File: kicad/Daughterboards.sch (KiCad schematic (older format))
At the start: 6 parts

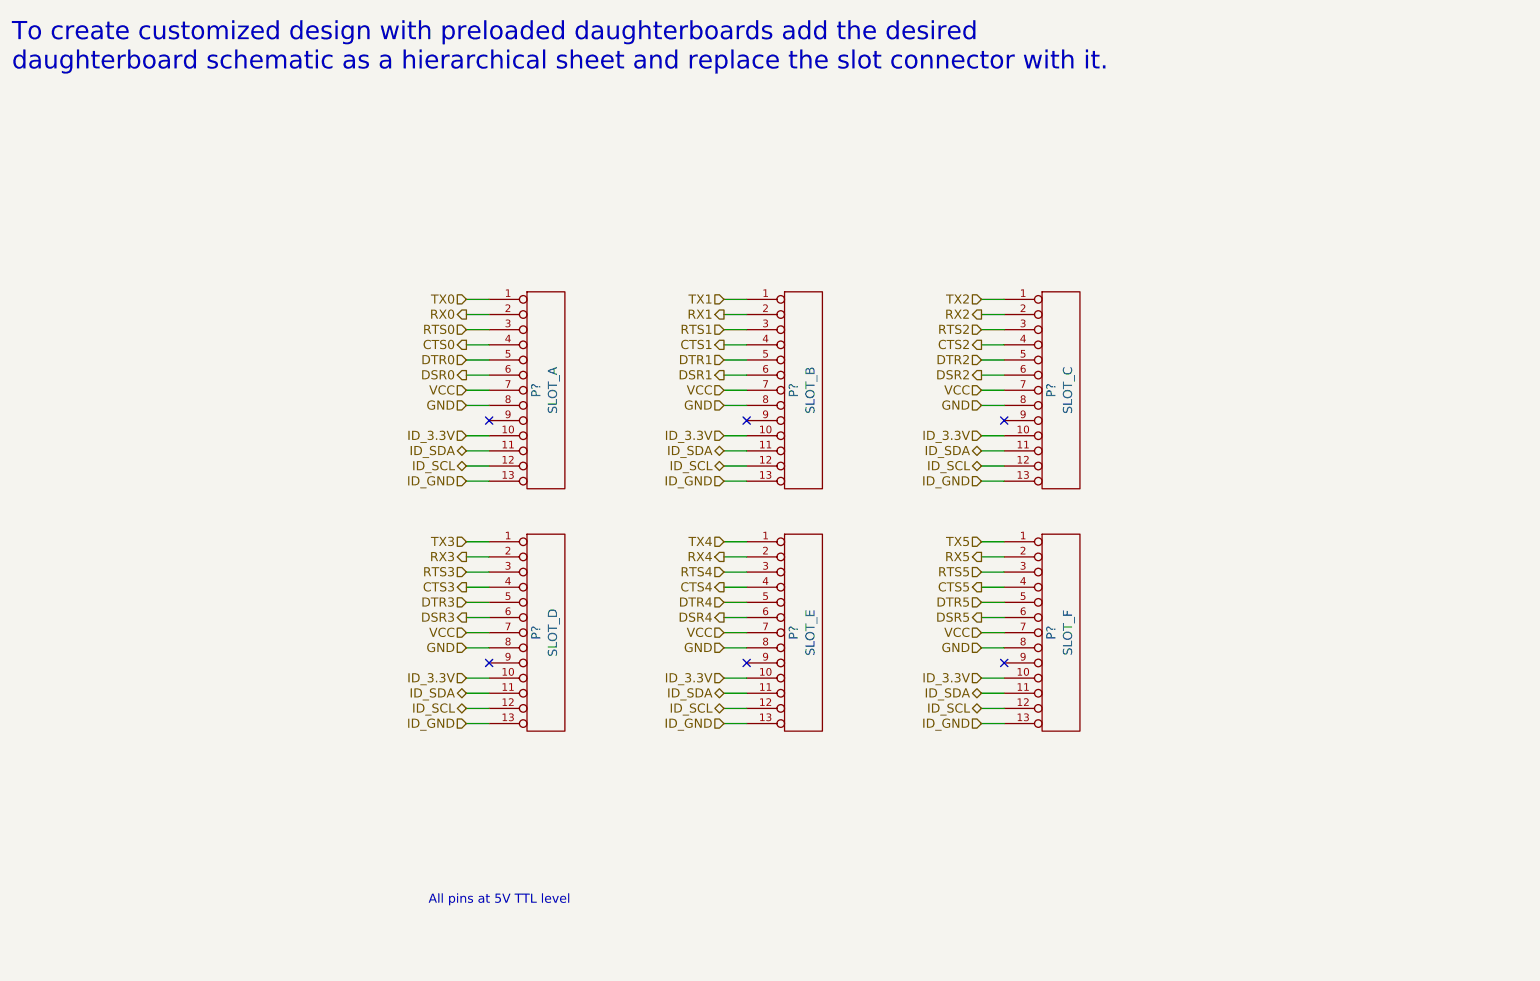
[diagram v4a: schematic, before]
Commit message: Completed PIC 18 USB sheet; Motherboard schematic done
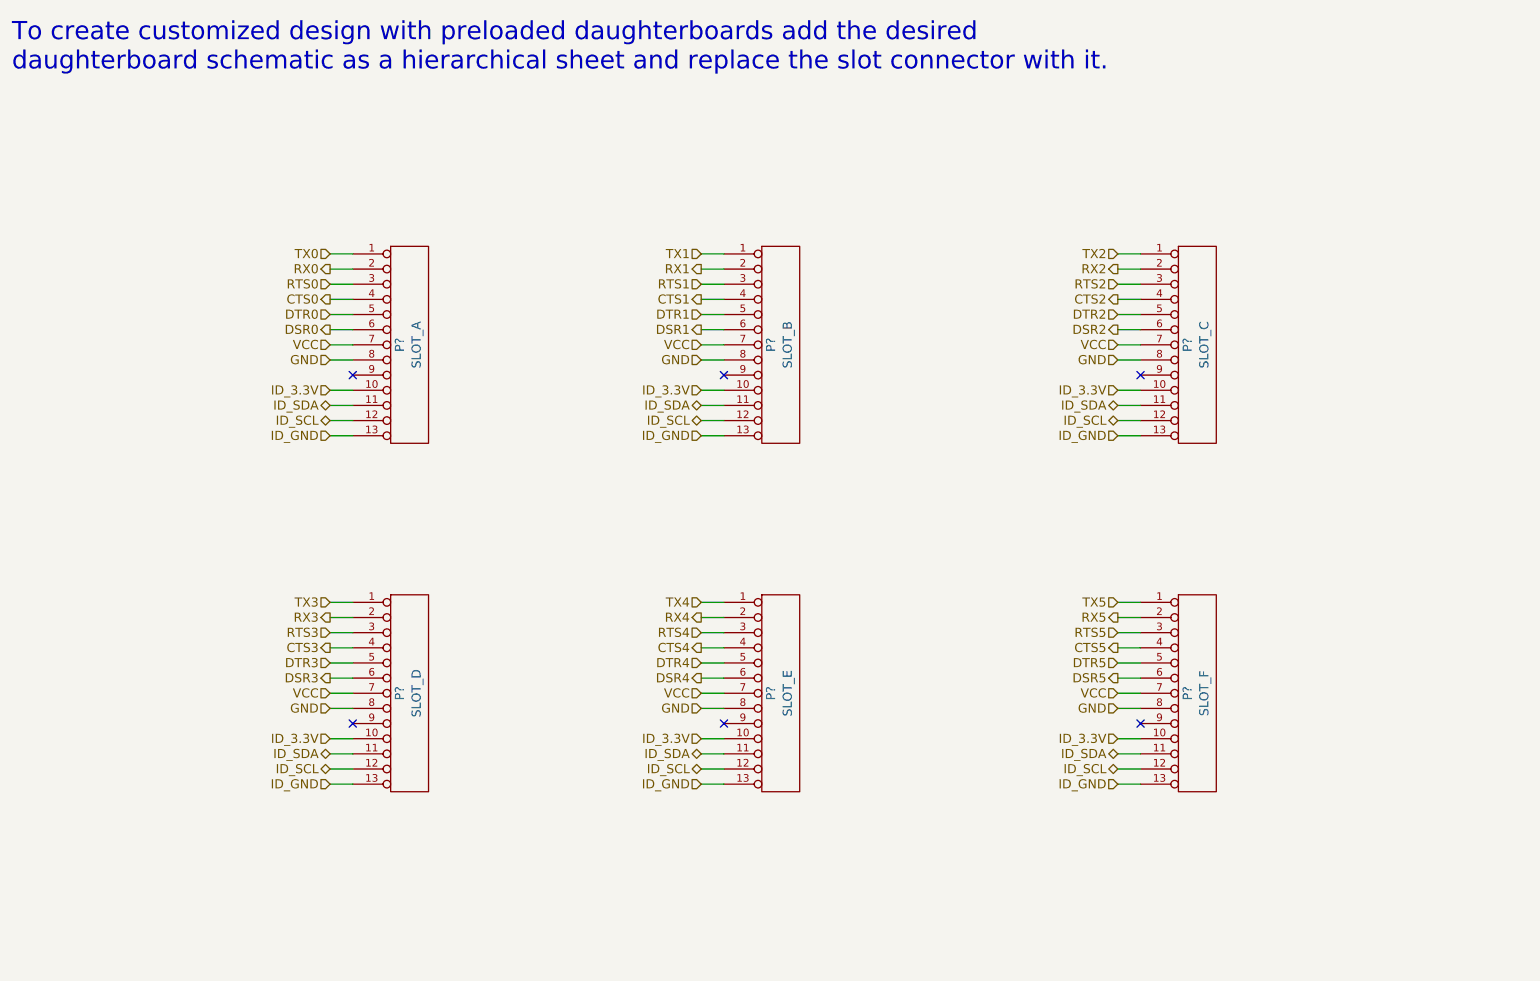
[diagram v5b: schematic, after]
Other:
- note removed: "All pins at 5V TTL level"
- moved on the sheet: P?

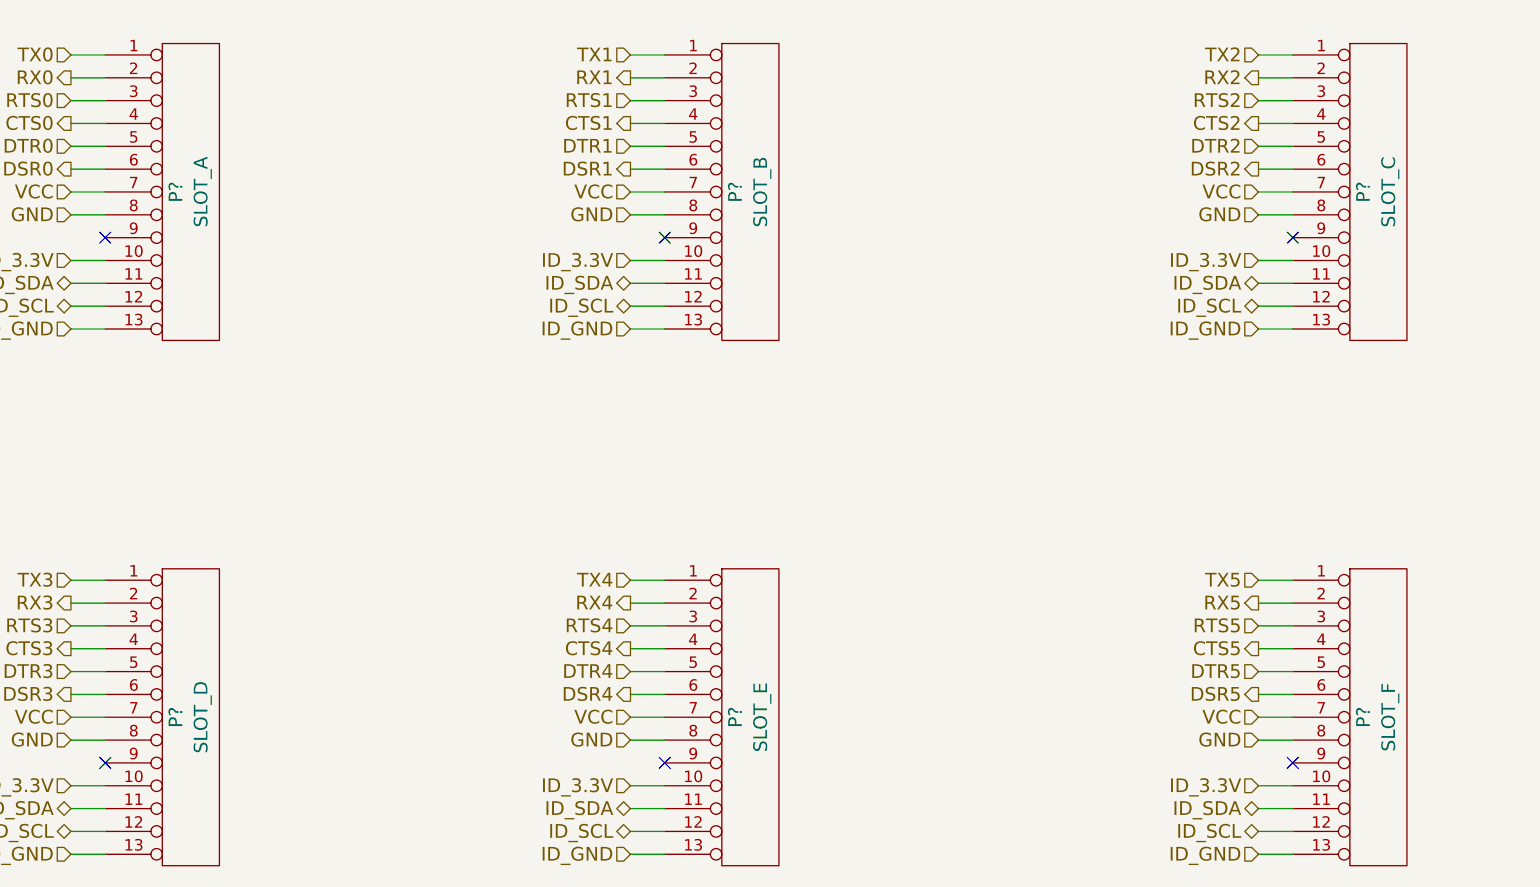
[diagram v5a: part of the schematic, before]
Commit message: Netlist DRC pass - fixed pins types, incorrect connections, added PWRFLAGS
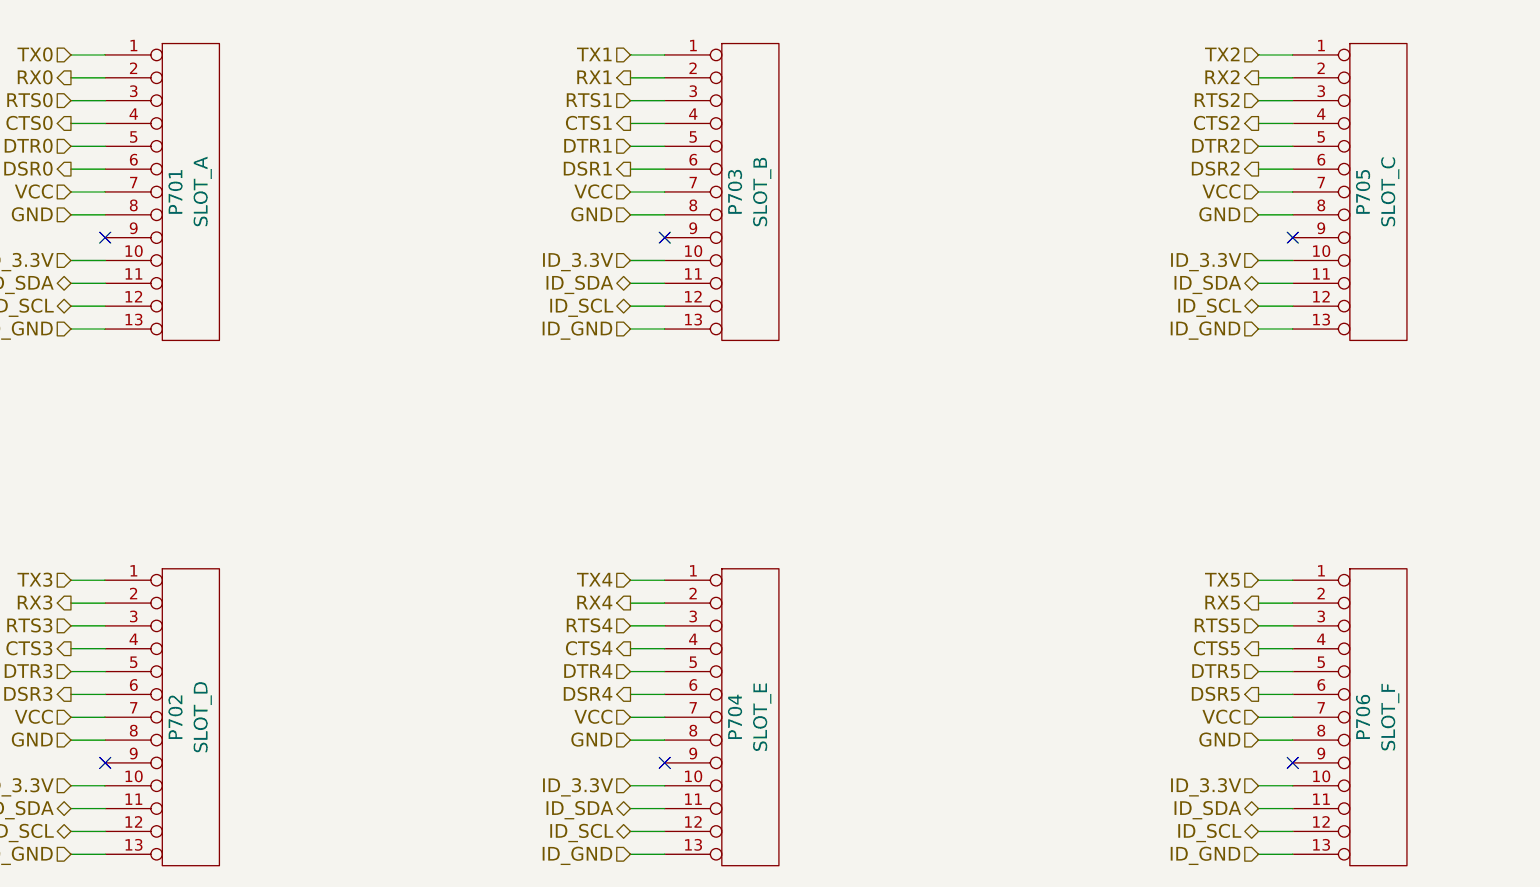
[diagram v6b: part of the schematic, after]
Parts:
- gave numbers to parts that had none: 6
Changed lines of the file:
@@
 	8300 5850 8450 5850
 $Comp
-L CONN_13 P?
+L CONN_13 P701
 U 1 1 53B751DE
 P 3600 2950
-F 0 "P?" V 3560 2950 60  0000 C CNN
+F 0 "P701" V 3560 2950 60  0000 C CNN
 F 1 "SLOT_A" V 3670 2950 60  0000 C CNN
 F 2 "" H 3600 2950 60  0000 C CNN
@@
 $EndComp
 $Comp
-L CONN_13 P?
+L CONN_13 P703
 U 1 1 53B751F7
 P 6050 2950
-F 0 "P?" V 6010 2950 60  0000 C CNN
+F 0 "P703" V 6010 2950 60  0000 C CNN
 F 1 "SLOT_B" V 6120 2950 60  0000 C CNN
 F 2 "" H 6050 2950 60  0000 C CNN
@@
 $EndComp
 $Comp
-L CONN_13 P?
+L CONN_13 P705
 U 1 1 53B75207
 P 8800 2950
-F 0 "P?" V 8760 2950 60  0000 C CNN
+F 0 "P705" V 8760 2950 60  0000 C CNN
 F 1 "SLOT_C" V 8870 2950 60  0000 C CNN
 F 2 "" H 8800 2950 60  0000 C CNN
@@
 $EndComp
 $Comp
-L CONN_13 P?
+L CONN_13 P702
 U 1 1 53B7520D
 P 3600 5250
-F 0 "P?" V 3560 5250 60  0000 C CNN
+F 0 "P702" V 3560 5250 60  0000 C CNN
 F 1 "SLOT_D" V 3670 5250 60  0000 C CNN
 F 2 "" H 3600 5250 60  0000 C CNN
@@
 $EndComp
 $Comp
-L CONN_13 P?
+L CONN_13 P704
 U 1 1 53B75213
 P 6050 5250
-F 0 "P?" V 6010 5250 60  0000 C CNN
+F 0 "P704" V 6010 5250 60  0000 C CNN
 F 1 "SLOT_E" V 6120 5250 60  0000 C CNN
 F 2 "" H 6050 5250 60  0000 C CNN
@@
 $EndComp
 $Comp
-L CONN_13 P?
+L CONN_13 P706
 U 1 1 53B75219
 P 8800 5250
-F 0 "P?" V 8760 5250 60  0000 C CNN
+F 0 "P706" V 8760 5250 60  0000 C CNN
 F 1 "SLOT_F" V 8870 5250 60  0000 C CNN
 F 2 "" H 8800 5250 60  0000 C CNN

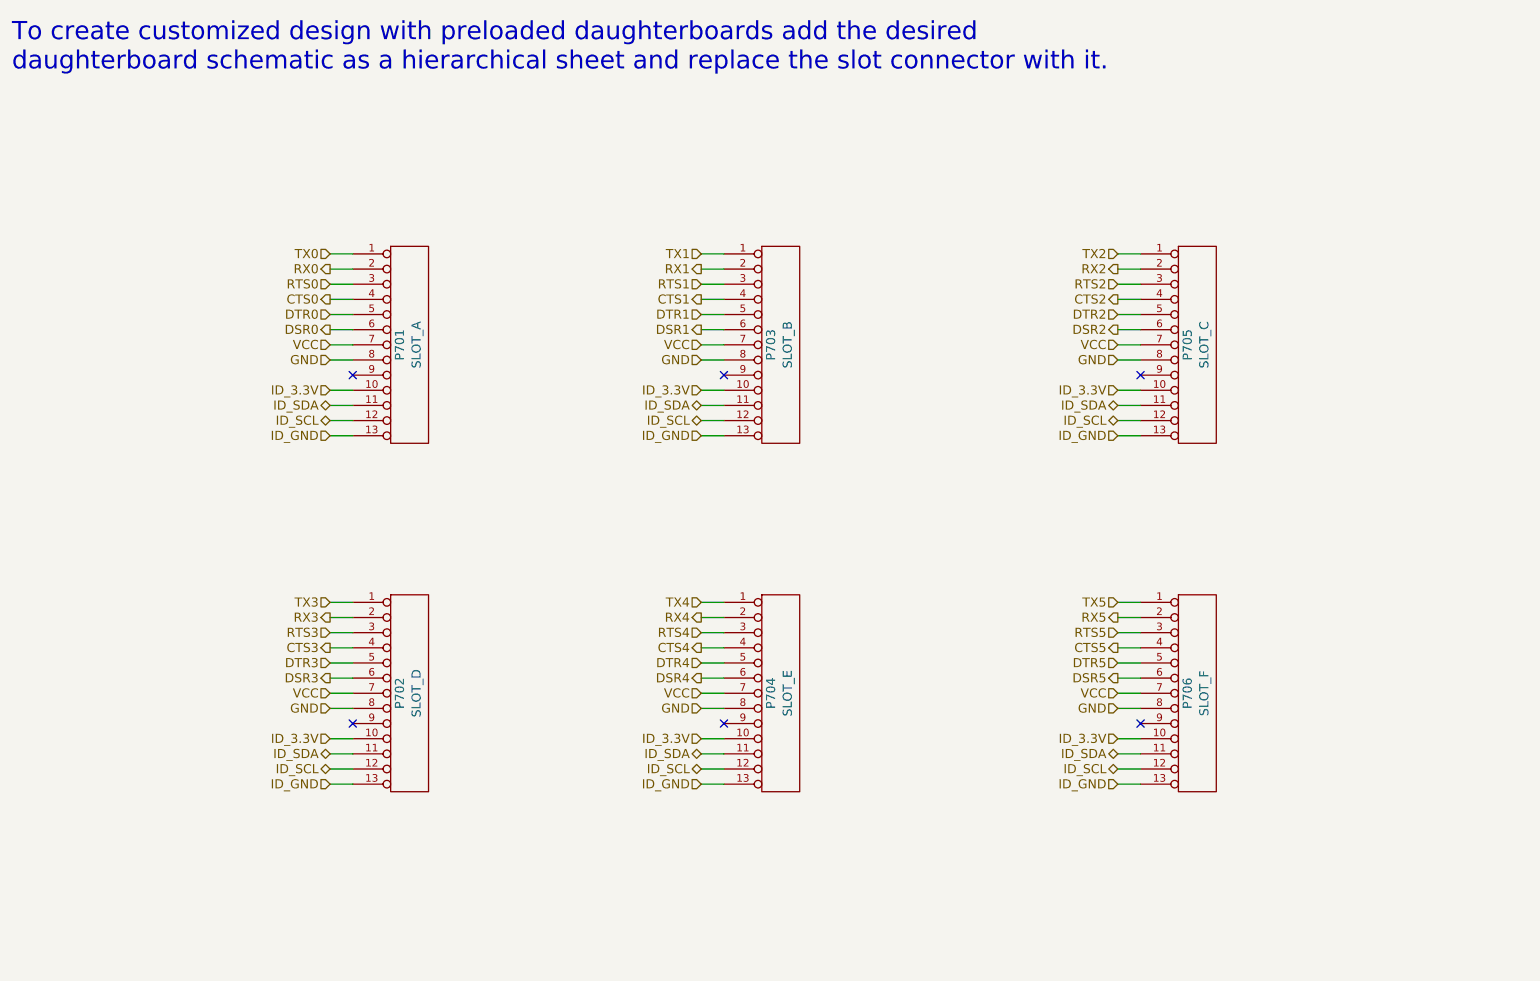
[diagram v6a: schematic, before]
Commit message: Fixed major flaw in autodetection circuit - daughterboard header pinout changed to set address of ROMs depending on slot
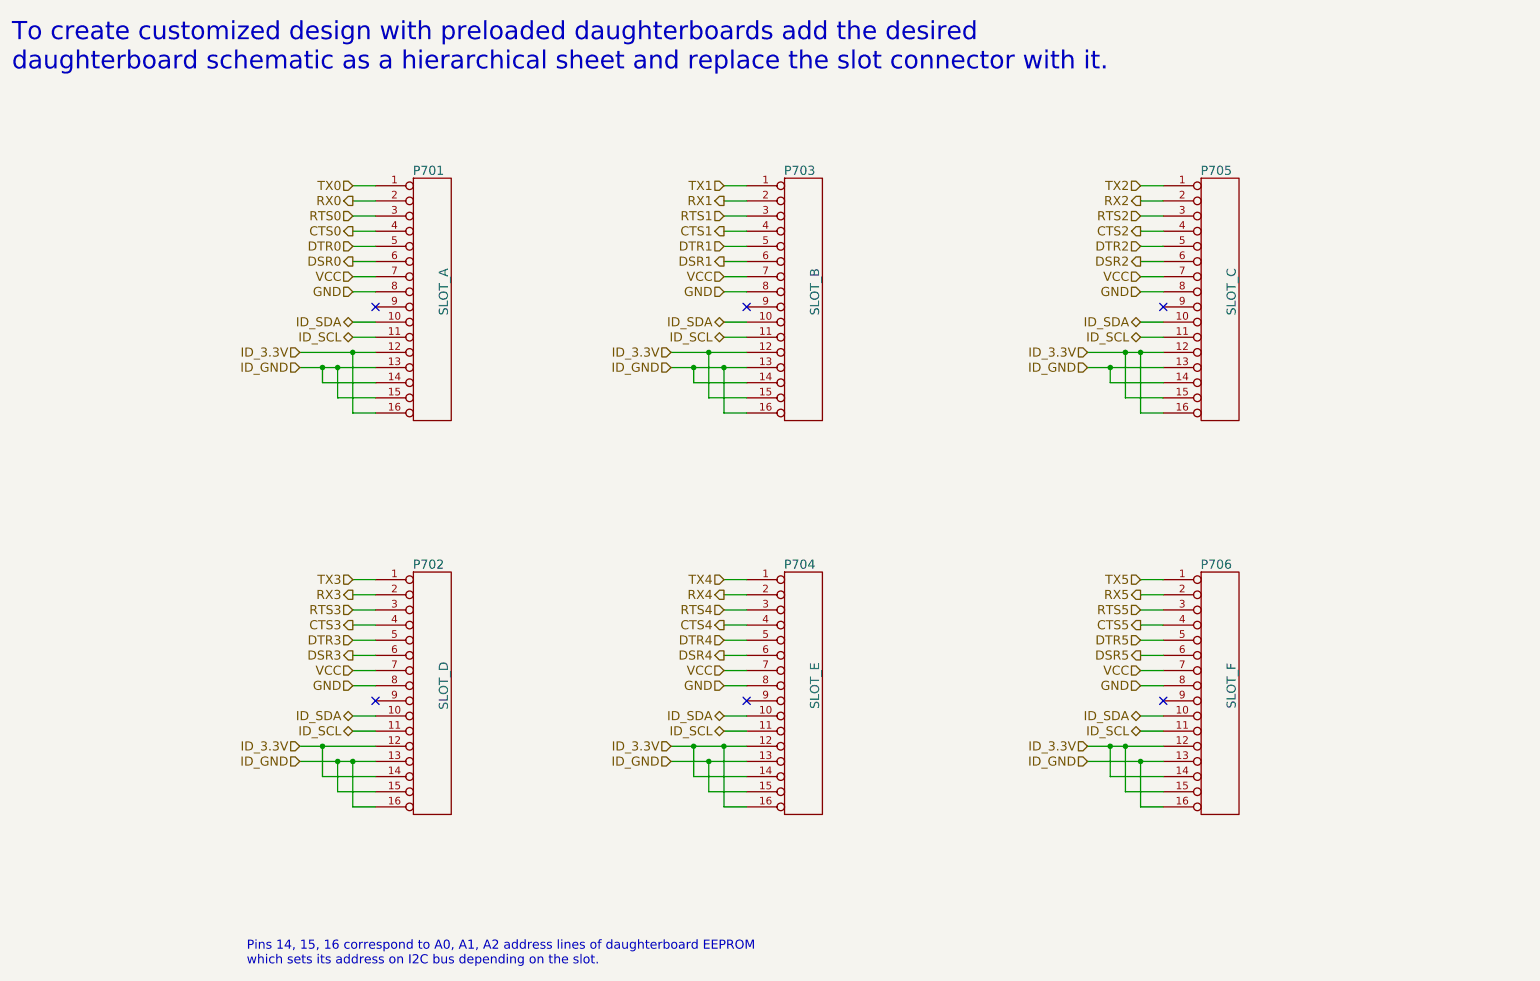
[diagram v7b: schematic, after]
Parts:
- removed P701: SLOT_A, symbol CONN_13
- removed P702: SLOT_D, symbol CONN_13
- removed P703: SLOT_B, symbol CONN_13
- removed P704: SLOT_E, symbol CONN_13
- removed P705: SLOT_C, symbol CONN_13
- removed P706: SLOT_F, symbol CONN_13
- added P701: SLOT_A, ~, symbol CONN_16
- added P702: SLOT_D, ~, symbol CONN_16
- added P703: SLOT_B, ~, symbol CONN_16
- added P704: SLOT_E, ~, symbol CONN_16
- added P705: SLOT_C, ~, symbol CONN_16
- added P706: SLOT_F, ~, symbol CONN_16
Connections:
- net CTS0: now also P701.4 (P4)
- net CTS1: now also P703.4 (P4)
- net CTS2: now also P705.4 (P4)
- net CTS3: now also P702.4 (P4)
- net CTS4: now also P704.4 (P4)
- net CTS5: now also P706.4 (P4)
- net DSR0: now also P701.6 (P6)
- net DSR1: now also P703.6 (P6)
- net DSR2: now also P705.6 (P6)
- net DSR3: now also P702.6 (P6)
- net DSR4: now also P704.6 (P6)
- net DSR5: now also P706.6 (P6)
- net DTR0: now also P701.5 (P5)
- net DTR1: now also P703.5 (P5)
- net DTR2: now also P705.5 (P5)
- net DTR3: now also P702.5 (P5)
- net DTR4: now also P704.5 (P5)
- net DTR5: now also P706.5 (P5)
- net GND: now also P701.8 (P8), P702.8 (P8), P703.8 (P8), P704.8 (P8), P705.8 (P8), P706.8 (P8)
- net ID_3.3V: now also P701.12 (P12), P701.16, P702.12 (P12), P702.14, P703.12 (P12), P703.15, P704.12 (P12), P704.14, P704.16, P705.12 (P12), P705.15, P705.16, P706.12 (P12), P706.14, P706.15
- net ID_GND: now also P701.13 (P13), P701.14, P701.15, P702.13 (P13), P702.15, P702.16, P703.13 (P13), P703.14, P703.16, P704.13 (P13), P704.15, P705.13 (P13), P705.14, P706.13 (P13), P706.16
- net ID_SCL: now also P701.11 (P11), P702.11 (P11), P703.11 (P11), P704.11 (P11), P705.11 (P11), P706.11 (P11)
- net ID_SDA: now also P701.10 (P10), P702.10 (P10), P703.10 (P10), P704.10 (P10), P705.10 (P10), P706.10 (P10)
- net RTS0: now also P701.3 (P3)
- net RTS1: now also P703.3 (P3)
- net RTS2: now also P705.3 (P3)
- net RTS3: now also P702.3 (P3)
- net RTS4: now also P704.3 (P3)
- net RTS5: now also P706.3 (P3)
- net RX0: now also P701.2 (P2)
- net RX1: now also P703.2 (P2)
- net RX2: now also P705.2 (P2)
- net RX3: now also P702.2 (P2)
- net RX4: now also P704.2 (P2)
- net RX5: now also P706.2 (P2)
- net TX0: now also P701.1 (P1)
- net TX1: now also P703.1 (P1)
- net TX2: now also P705.1 (P1)
- net TX3: now also P702.1 (P1)
- net TX4: now also P704.1 (P1)
- net TX5: now also P706.1 (P1)
- net VCC: now also P701.7 (P7), P702.7 (P7), P703.7 (P7), P704.7 (P7), P705.7 (P7), P706.7 (P7)
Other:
- note added: "Pins 14, 15, 16 correspond to A0, A1, A2 address lines of daughterboard EEPROM \nwhich sets its address on I2C bus depending on the slot."
